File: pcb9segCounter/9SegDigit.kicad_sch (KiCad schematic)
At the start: 18 parts

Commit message: Everything looks good for manufacture
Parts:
- added C8: 0.1u, Capacitor_SMD:C_0805_2012Metric, symbol Device:C
- renumbered C9 to C10, C10 to C11, C11 to C12, C12 to C13, C13 to C14, C14 to C15, C15 to C16, C16 to C18
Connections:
- net 5V: now also C8.1
- net GND: now also C8.2
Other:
- moved on the sheet: C16
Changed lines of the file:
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@@
 	)
 	(junction
-		(at 158.75 133.35)
+		(at 149.86 133.35)
 		(diameter 0)
 		(color 0 0 0 0)
 	)
 	(junction
-		(at 158.75 140.97)
+		(at 167.64 133.35)
+		(diameter 0)
+		(color 0 0 0 0)
+	)
+	(junction
+		(at 149.86 140.97)
 		(diameter 0)
 		(color 0 0 0 0)
@@
 	)
 	(junction
+		(at 167.64 140.97)
+		(diameter 0)
+		(color 0 0 0 0)
+	)
+	(junction
 		(at 132.08 99.06)
 		(diameter 0)
@@
 	(wire
 		(pts
-			(xy 158.75 133.35) (xy 185.42 133.35)
-		)
-		(stroke
-			(width 0)
-			(type default)
-		)
-	)
-	(wire
-		(pts
-			(xy 132.08 133.35) (xy 158.75 133.35)
+			(xy 132.08 133.35) (xy 149.86 133.35)
+		)
+		(stroke
+			(width 0)
+			(type default)
+		)
+	)
+	(wire
+		(pts
+			(xy 167.64 140.97) (xy 185.42 140.97)
 		)
 		(stroke
@@
 	(wire
 		(pts
-			(xy 132.08 140.97) (xy 158.75 140.97)
+			(xy 132.08 140.97) (xy 149.86 140.97)
 		)
 		(stroke
@@
 	(wire
 		(pts
+			(xy 149.86 140.97) (xy 167.64 140.97)
+		)
+		(stroke
+			(width 0)
+			(type default)
+		)
+	)
+	(wire
+		(pts
 			(xy 149.86 114.3) (xy 132.08 114.3)
 		)
@@
 	(wire
 		(pts
+			(xy 149.86 133.35) (xy 167.64 133.35)
+		)
+		(stroke
+			(width 0)
+			(type default)
+		)
+	)
+	(wire
+		(pts
 			(xy 96.52 99.06) (xy 114.3 99.06)
 		)
@@
 	(wire
 		(pts
+			(xy 167.64 133.35) (xy 185.42 133.35)
+		)
+		(stroke
+			(width 0)
+			(type default)
+		)
+	)
+	(wire
+		(pts
 			(xy 96.52 114.3) (xy 78.74 114.3)
-		)
-		(stroke
-			(width 0)
-			(type default)
-		)
-	)
-	(wire
-		(pts
-			(xy 158.75 140.97) (xy 185.42 140.97)
 		)
 		(stroke
@@
 		(on_board yes)
 		(dnp no)
-		(property "Reference" "C9"
+		(property "Reference" "C10"
 			(at 46.99 135.8899 0)
 			(effects
@@
 			(project ""
 				(path "/c50b0073-6340-498a-8f0c-212ef3b3c0fe/3b31bf75-0830-4091-8274-a65747ea74f2"
-					(reference "C9")
+					(reference "C10")
 					(unit 1)
 				)
@@
 	(symbol
 		(lib_id "Device:C")
-		(at 158.75 137.16 0)
+		(at 149.86 137.16 0)
 		(unit 1)
 		(exclude_from_sim no)
@@
 		(dnp no)
 		(fields_autoplaced yes)
-		(property "Reference" "C15"
-			(at 162.56 135.8899 0)
+		(property "Reference" "C16"
+			(at 153.67 135.8899 0)
 			(effects
 				(font
@@
 		)
 		(property "Value" "0.1u"
-			(at 162.56 138.4299 0)
+			(at 153.67 138.4299 0)
 			(effects
 				(font
@@
 		)
 		(property "Footprint" "Capacitor_SMD:C_0805_2012Metric"
-			(at 159.7152 140.97 0)
+			(at 150.8252 140.97 0)
 			(effects
 				(font
@@
 		)
 		(property "Datasheet" "~"
-			(at 158.75 137.16 0)
+			(at 149.86 137.16 0)
 			(effects
 				(font
@@
 		)
 		(property "Description" "Unpolarized capacitor"
-			(at 158.75 137.16 0)
+			(at 149.86 137.16 0)
 			(effects
 				(font
@@
 		)
 		(property "Footprint Check" ""
-			(at 158.75 137.16 0)
+			(at 149.86 137.16 0)
 			(effects
 				(font
@@
 		)
 		(property "Implementation" ""
-			(at 158.75 137.16 0)
+			(at 149.86 137.16 0)
 			(effects
 				(font
@@
 		)
 		(property "footprintCheck" "y"
-			(at 158.75 137.16 0)
+			(at 149.86 137.16 0)
 			(effects
 				(font
@@
 		)
 		(property "implementationCheck" "y"
-			(at 158.75 137.16 0)
+			(at 149.86 137.16 0)
 			(effects
 				(font
@@
 			(project "pcb9segCounter"
 				(path "/c50b0073-6340-498a-8f0c-212ef3b3c0fe/3b31bf75-0830-4091-8274-a65747ea74f2"
-					(reference "C15")
+					(reference "C16")
 					(unit 1)
 				)
 				(path "/c50b0073-6340-498a-8f0c-212ef3b3c0fe/5c493882-1689-4a6d-b4b4-08608e8edf66"
 					(reference "C7")
+					(unit 1)
+				)
+			)
+		)
+	)
+	(symbol
+		(lib_id "Device:C")
+		(at 167.64 137.16 0)
+		(unit 1)
+		(exclude_from_sim no)
+		(in_bom yes)
+		(on_board yes)
+		(dnp no)
+		(fields_autoplaced yes)
+		(property "Reference" "C8"
+			(at 171.45 135.8899 0)
+			(effects
+				(font
+					(size 1.27 1.27)
+				)
+				(justify left)
+			)
+		)
+		(property "Value" "0.1u"
+			(at 171.45 138.4299 0)
+			(effects
+				(font
+					(size 1.27 1.27)
+				)
+				(justify left)
+			)
+		)
+		(property "Footprint" "Capacitor_SMD:C_0805_2012Metric"
+			(at 168.6052 140.97 0)
+			(effects
+				(font
+					(size 1.27 1.27)
+				)
+				(hide yes)
+			)
+		)
+		(property "Datasheet" "~"
+			(at 167.64 137.16 0)
+			(effects
+				(font
+					(size 1.27 1.27)
+				)
+				(hide yes)
+			)
+		)
+		(property "Description" "Unpolarized capacitor"
+			(at 167.64 137.16 0)
+			(effects
+				(font
+					(size 1.27 1.27)
+				)
+				(hide yes)
+			)
+		)
+		(property "Footprint Check" ""
+			(at 167.64 137.16 0)
+			(effects
+				(font
+					(size 1.27 1.27)
+				)
+				(hide yes)
+			)
+		)
+		(property "Implementation" ""
+			(at 167.64 137.16 0)
+			(effects
+				(font
+					(size 1.27 1.27)
+				)
+				(hide yes)
+			)
+		)
+		(property "footprintCheck" "y"
+			(at 167.64 137.16 0)
+			(effects
+				(font
+					(size 1.27 1.27)
+				)
+				(hide yes)
+			)
+		)
+		(property "implementationCheck" "y"
+			(at 167.64 137.16 0)
+			(effects
+				(font
+					(size 1.27 1.27)
+				)
+				(hide yes)
+			)
+		)
+		(pin "2"
+		)
+		(pin "1"
+		)
+		(instances
+			(project "pcb9segCounter"
+				(path "/c50b0073-6340-498a-8f0c-212ef3b3c0fe/3b31bf75-0830-4091-8274-a65747ea74f2"
+					(reference "C17")
+					(unit 1)
+				)
+				(path "/c50b0073-6340-498a-8f0c-212ef3b3c0fe/5c493882-1689-4a6d-b4b4-08608e8edf66"
+					(reference "C8")
 					(unit 1)
 				)
@@
 		(dnp no)
 		(fields_autoplaced yes)
-		(property "Reference" "C13"
+		(property "Reference" "C14"
 			(at 118.11 135.8899 0)
 			(effects
@@
 			(project "pcb9segCounter"
 				(path "/c50b0073-6340-498a-8f0c-212ef3b3c0fe/3b31bf75-0830-4091-8274-a65747ea74f2"
-					(reference "C13")
+					(reference "C14")
 					(unit 1)
 				)
@@
 		(dnp no)
 		(fields_autoplaced yes)
-		(property "Reference" "C14"
+		(property "Reference" "C15"
 			(at 135.89 135.8899 0)
 			(effects
@@
 			(project "pcb9segCounter"
 				(path "/c50b0073-6340-498a-8f0c-212ef3b3c0fe/3b31bf75-0830-4091-8274-a65747ea74f2"
-					(reference "C14")
+					(reference "C15")
 					(unit 1)
 				)
@@
 		(dnp no)
 		(fields_autoplaced yes)
-		(property "Reference" "C10"
+		(property "Reference" "C11"
 			(at 64.77 135.8899 0)
 			(effects
@@
 			(project "pcb9segCounter"
 				(path "/c50b0073-6340-498a-8f0c-212ef3b3c0fe/3b31bf75-0830-4091-8274-a65747ea74f2"
-					(reference "C10")
+					(reference "C11")
 					(unit 1)
 				)
@@
 		(dnp no)
 		(fields_autoplaced yes)
-		(property "Reference" "C16"
+		(property "Reference" "C18"
 			(at 189.23 135.8899 0)
 			(effects
@@
 			(project "pcb9segCounter"
 				(path "/c50b0073-6340-498a-8f0c-212ef3b3c0fe/3b31bf75-0830-4091-8274-a65747ea74f2"
-					(reference "C16")
+					(reference "C18")
 					(unit 1)
 				)
 				(path "/c50b0073-6340-498a-8f0c-212ef3b3c0fe/5c493882-1689-4a6d-b4b4-08608e8edf66"
-					(reference "C8")
+					(reference "C9")
 					(unit 1)
 				)
@@
 		(dnp no)
 		(fields_autoplaced yes)
-		(property "Reference" "C11"
+		(property "Reference" "C12"
 			(at 82.55 135.8899 0)
 			(effects
@@
 			(project "pcb9segCounter"
 				(path "/c50b0073-6340-498a-8f0c-212ef3b3c0fe/3b31bf75-0830-4091-8274-a65747ea74f2"
-					(reference "C11")
+					(reference "C12")
 					(unit 1)
 				)
@@
 		(dnp no)
 		(fields_autoplaced yes)
-		(property "Reference" "C12"
+		(property "Reference" "C13"
 			(at 100.33 135.8899 0)
 			(effects
@@
 			(project "pcb9segCounter"
 				(path "/c50b0073-6340-498a-8f0c-212ef3b3c0fe/3b31bf75-0830-4091-8274-a65747ea74f2"
-					(reference "C12")
-					(unit 1)
-				)
+					(reference "C13")
+					(unit 1)
+				)

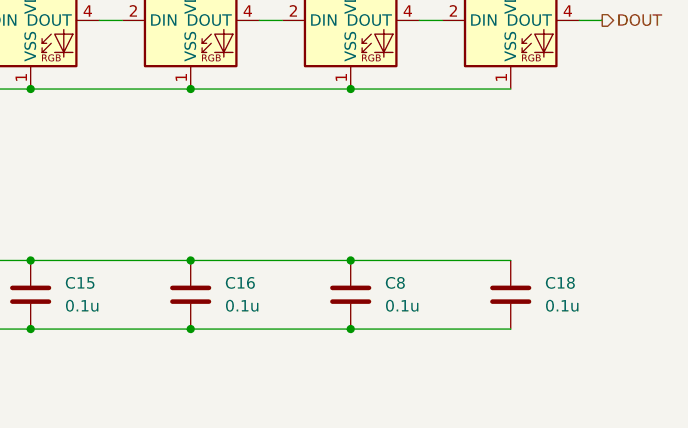
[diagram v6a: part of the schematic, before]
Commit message: Updated details to export BOM
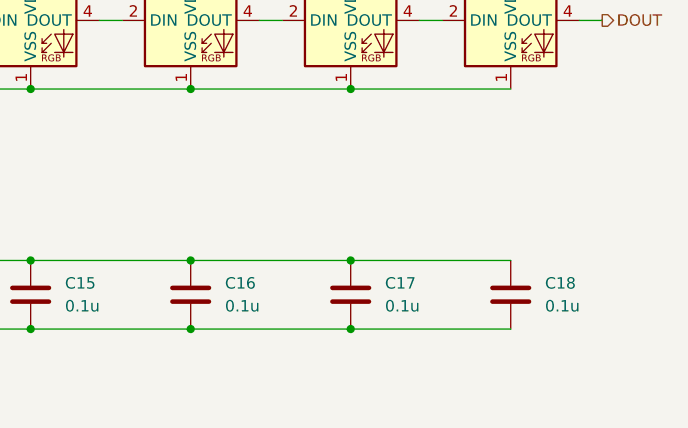
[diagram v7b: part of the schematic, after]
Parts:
- renumbered C8 to C17
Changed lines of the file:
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@@
 		)
 		(instances
-			(project ""
+			(project "pcb9segCounter"
 				(path "/c50b0073-6340-498a-8f0c-212ef3b3c0fe/3b31bf75-0830-4091-8274-a65747ea74f2"
 					(reference "C10")
@@
 		(dnp no)
 		(fields_autoplaced yes)
-		(property "Reference" "C8"
+		(property "Reference" "C17"
 			(at 171.45 135.8899 0)
 			(effects
